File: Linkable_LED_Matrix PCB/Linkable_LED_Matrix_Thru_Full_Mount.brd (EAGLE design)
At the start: 32 x 32 mm, 9 parts, among them J1 AVR_SPI_PRG_6NS

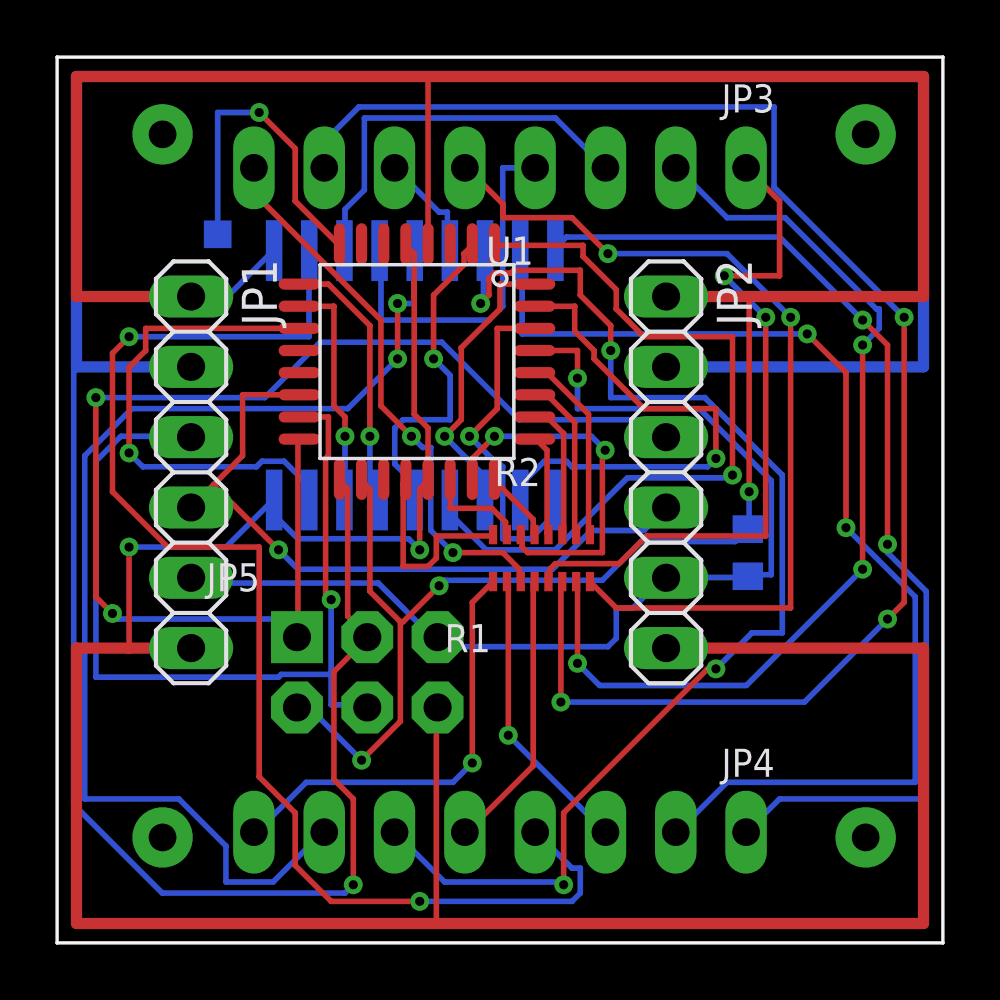
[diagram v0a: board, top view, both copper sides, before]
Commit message: Fixed silk screen and shifted JP2 very slightly
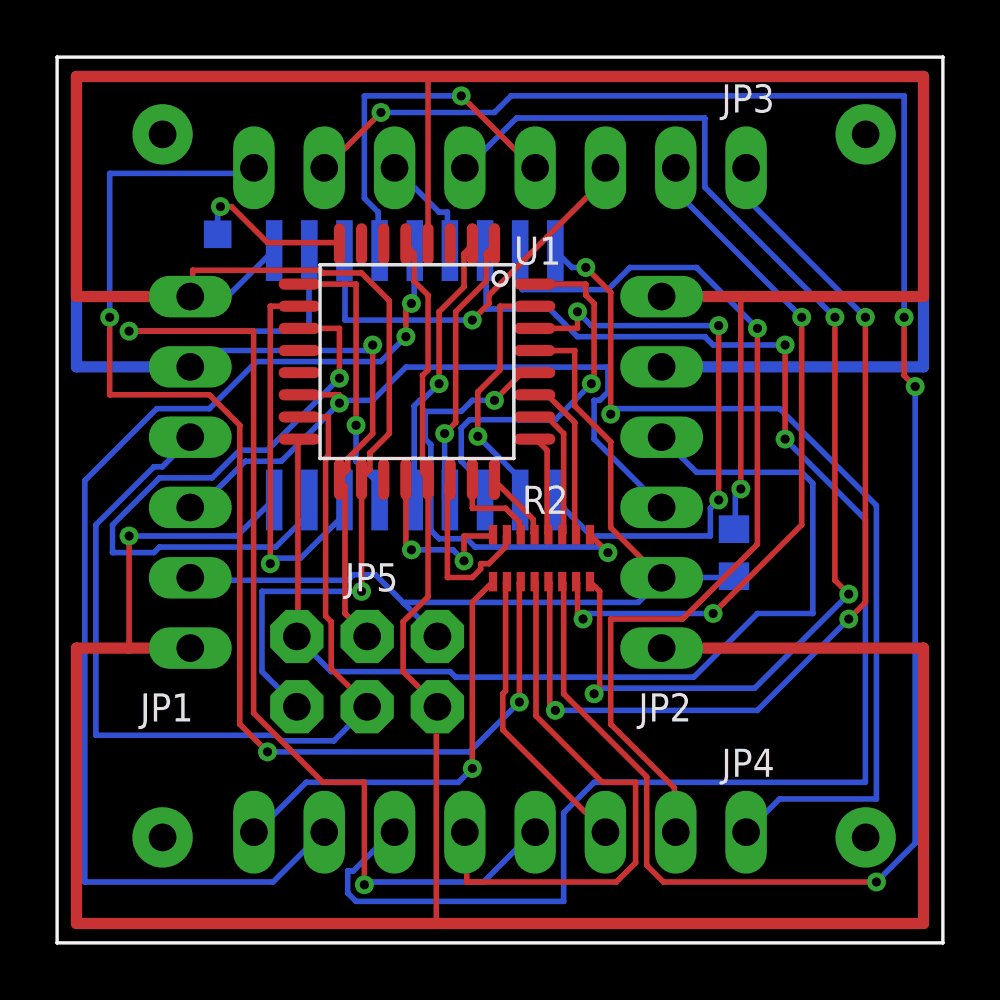
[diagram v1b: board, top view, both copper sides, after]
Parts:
- removed J1: AVR_SPI_PRG_6NS, SparkFun-Connectors:2X3-NS
- removed JP1, JP2: (no value), pinhead:1X06
- added U$6, U$7: DIP1X6MALE, ScottSilver:DIP1X6MALE
- added U$9: DIP2X3MALE, ScottSilver:DIP2X3MALE
- moved R1 0.50 mm to (24.5, 14.1)
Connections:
- net CS: now also U$6.3, U$7.3; no longer JP1.4, JP2.4
- net GND: now also U$6.1, U$7.1, U$9.GND; no longer J1.6, JP1.6, JP2.6
- net MISO: now also U$7.4, U$9.MISO; no longer J1.1, JP2.3
- net MOSI: now also U$6.4, U$9.MOSI; no longer J1.4, JP1.3
- net RESET: now also U$6.2, U$7.2, U$9.RESET; no longer J1.5, JP1.5, JP2.5
- net SCK: now also U$6.5, U$7.5, U$9.SCK; no longer J1.3, JP1.2, JP2.2
- net VCC: now also U$6.6, U$7.6, U$9.5V; no longer J1.2, JP1.1, JP2.1
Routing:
- net SCK: track 108.3 -> 83.5 mm
- net N$30: track 20.2 -> 44.9 mm, vias 2 -> 3
- net COL3: track 28.0 -> 10.2 mm
- net N$27: track 55.9 -> 71.2 mm, vias 3 -> 4
- net N$3: track 44.7 -> 56.0 mm, vias 4 -> 2
- net N$25: track 32.4 -> 43.7 mm, vias 2 -> 3
- net N$29: track 10.1 -> 20.6 mm
- net N$28: track 25.2 -> 35.1 mm, vias 2 -> 3
- net ROW2: track 13.3 -> 3.43 mm, vias 2 -> 0
- net ROW7: track 6.94 -> 16.6 mm, vias 0 -> 2
- net COL1: track 18.8 -> 9.23 mm
- net N$26: track 34.5 -> 25.6 mm
- net COL0: track 12.7 -> 21.3 mm, vias 1 -> 3
- net MISO: track 45.1 -> 38.3 mm, vias 2 -> 0
- net N$2: track 40.6 -> 34.1 mm, vias 2 -> 1
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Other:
- board text added: "JP1"
- board text added: "JP2"

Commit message: Added bypass cap and removed deprecated seperate resistor design
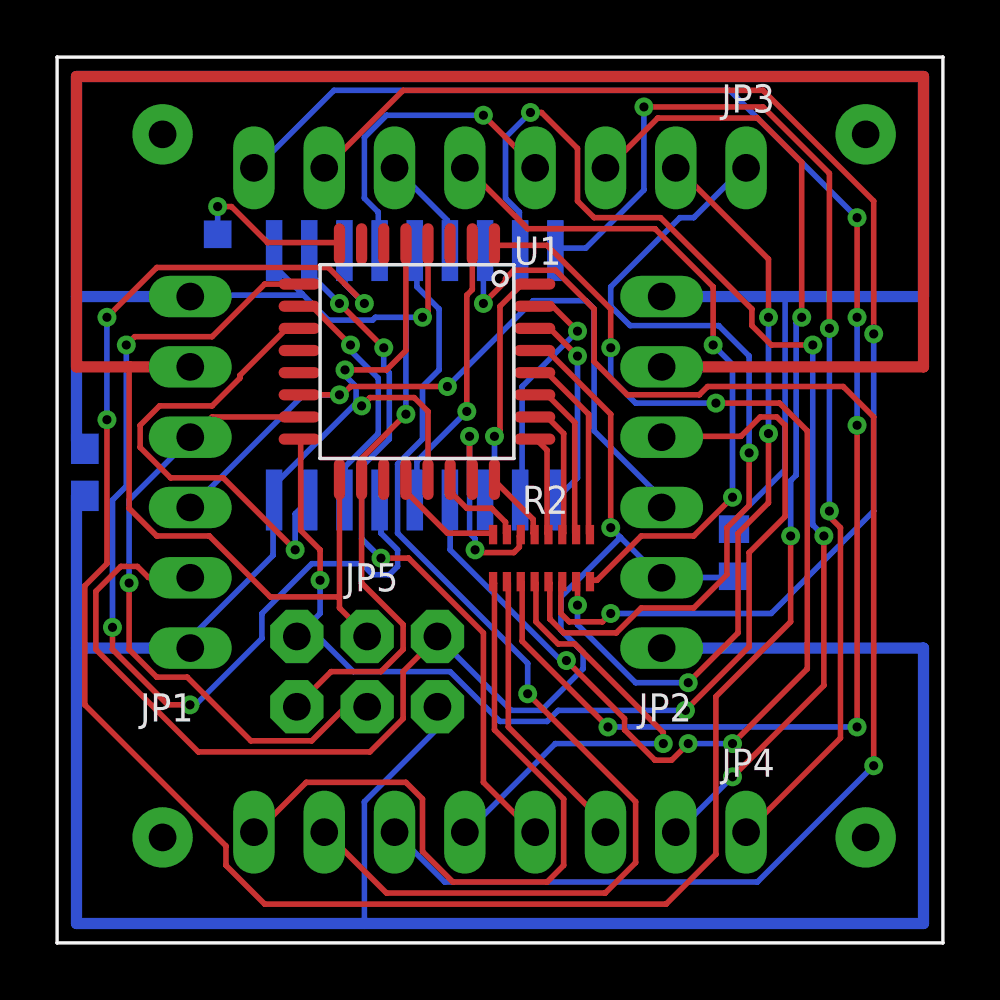
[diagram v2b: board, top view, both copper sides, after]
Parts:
- added C1: 1uF, resistor:C0603
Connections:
- net GND: now also C1.2
- net VCC: now also C1.1
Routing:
- net N$7: track 14.6 -> 88.8 mm, vias 1 -> 5
- net COL3: track 10.2 -> 43.6 mm, vias 1 -> 5
- net COL5: track 10.2 -> 35.1 mm, vias 1 -> 3
- net N$27: track 71.2 -> 48.1 mm, vias 4 -> 2
- net N$25: track 43.7 -> 25.1 mm, vias 3 -> 2
- net N$8: track 43.4 -> 25.9 mm, vias 2 -> 3
- net RESET: track 33.3 -> 48.6 mm, vias 0 -> 1
- net N$30: track 44.9 -> 58.8 mm, vias 3 -> 5
- net COL0: track 21.3 -> 7.50 mm, vias 3 -> 1
- net MOSI: track 34.9 -> 23.3 mm, vias 0 -> 1
- net N$32: track 15.9 -> 26.1 mm, vias 1 -> 0
- net ROW7: track 16.6 -> 6.94 mm, vias 2 -> 0
- net N$2: track 34.1 -> 40.7 mm, vias 1 -> 4
- net N$1: track 34.0 -> 40.2 mm, vias 2 -> 3
- net COL7: track 22.8 -> 17.2 mm
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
